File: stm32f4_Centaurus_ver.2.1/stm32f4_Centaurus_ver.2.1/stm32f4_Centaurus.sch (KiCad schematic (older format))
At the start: 215 parts, among them IC1 PIC24FJ64GB004, P1 PICKit3, P10 XA2_12V, P11 CAN0, P12 CAN1, P13 CAN0, P14 CAN1, P15 SERIAL2, P16 SERIAL0, P17 XA2_5V, P18 SWD, P2 SERIAL5_SBDBT, P23 A/D, P24 PWM, P25 A/D_batt, P26 PWM_batt, P27 EMERGENCY_CHECK, P28 I/O_5V, P29 I/O_Variable, P3 ENC0, P30 I/O_5V_batt, P31 I/O_Variable, P4 ENC2, P5 SERIAL1, P6 ENC3, P7 ENC1, P8 SERIAL4, P9 SERIAL3, Q1 FET_P, Q2 FET_P, Q3 FET_P, Q4 NPN, Q5 NPN, Q6 FET_P, Q7 FET_N, SW1 Main_POWER, SW2 SW1, SW3 SW0, SW4 SW2, SW5 SW3, U1 STM32F407VG, U10 LOGO, U12 25LC010A, U13 LOGO, U2 AZ1086H, U3 MCP2221A, U4 BD9G101G, U5 MAX3051, U6 MAX3051, U7 AQM1602_BL, U8 OSTBABS4C2B, U9 LOGO, X1 8MHz

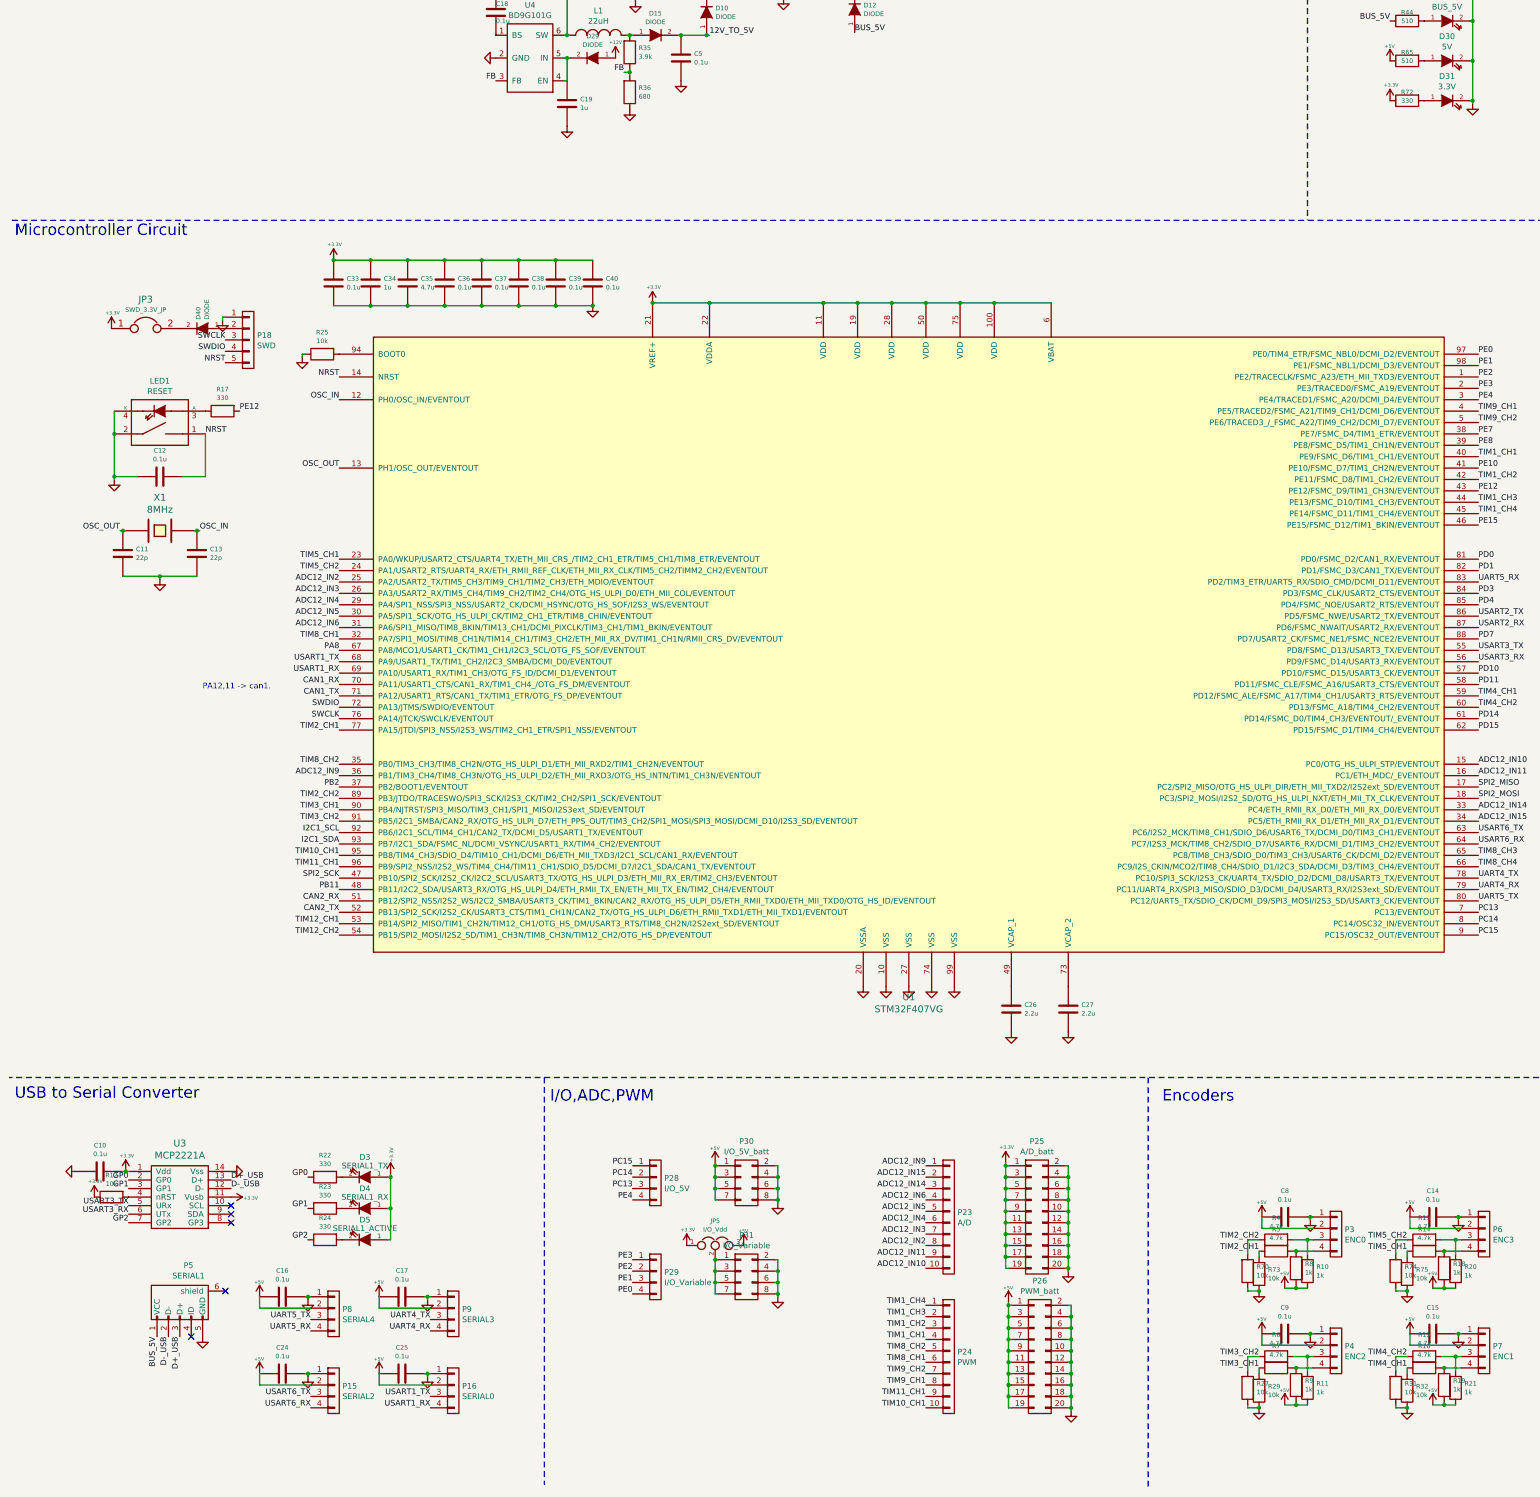
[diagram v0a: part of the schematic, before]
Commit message: Main typeC化
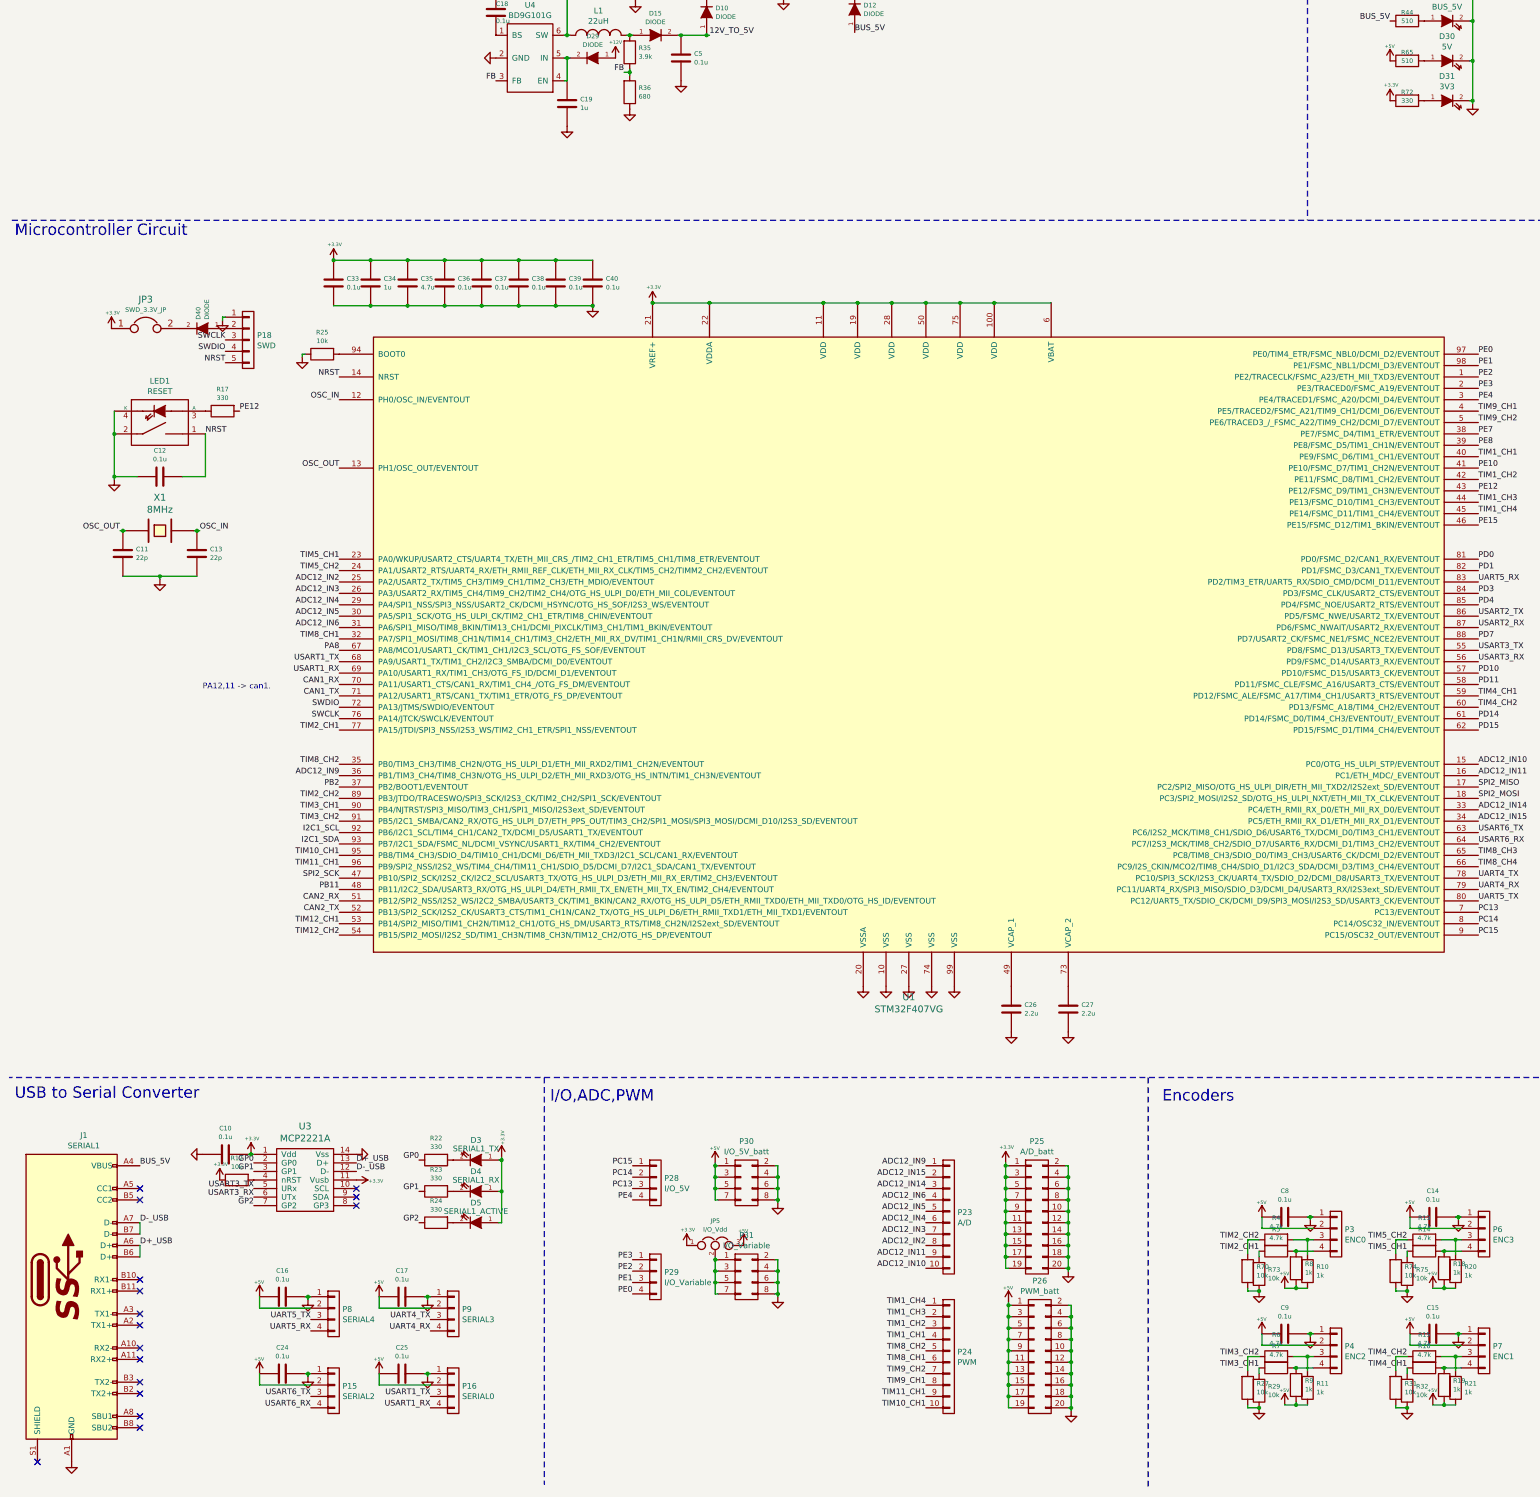
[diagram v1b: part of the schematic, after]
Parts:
- removed P5: SERIAL1, Mizz_lib:USB_Micro-B_Molex_47346-0001, symbol stm32f4_Centaurus-rescue:USB_OTG-conn
- added J1: SERIAL1, Connector_USB:USB_C_Receptacle_Palconn_UTC16-G, symbol Connector:USB_C_Receptacle
- D31: value 3.3V -> 3V3
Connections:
- net BUS_5V: now also J1.A4 (VBUS), J1.A9 (VBUS), J1.B4 (VBUS), J1.B9 (VBUS)
- net D+_USB: now also J1.A6 (D+), J1.B6 (D+)
- net D-_USB: now also J1.A7 (D-), J1.B7 (D-)
- net GND: now also J1.A1 (GND), J1.A12 (GND), J1.B1 (GND), J1.B12 (GND)
- no-connect marks 35 -> 46
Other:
- moved on the sheet: C10, D3, D4, D5, R12, R22, R23, R24, U3
